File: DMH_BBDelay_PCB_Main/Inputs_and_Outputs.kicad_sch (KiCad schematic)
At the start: 13 parts, among them J10 TRS_Jack_6.35mm_Sw, J11 TRS_Jack_6.35mm_Sw, J12 TRS_Jack_6.35mm_Sw, J13 TRS_Jack_6.35mm_Sw, J14 TRS_Jack_6.35mm_Sw, J15 TRS_Jack_6.35mm_Sw, J16 TRS_Jack_6.35mm_Sw, J17 TRS_Jack_6.35mm_Sw, J18 TRS_Jack_6.35mm_Sw, J19 TRS_Jack_6.35mm_Sw, J20 TRS_Jack_6.35mm_Sw, J200 IDC_02x05, J21 TRS_Jack_6.35mm_Sw

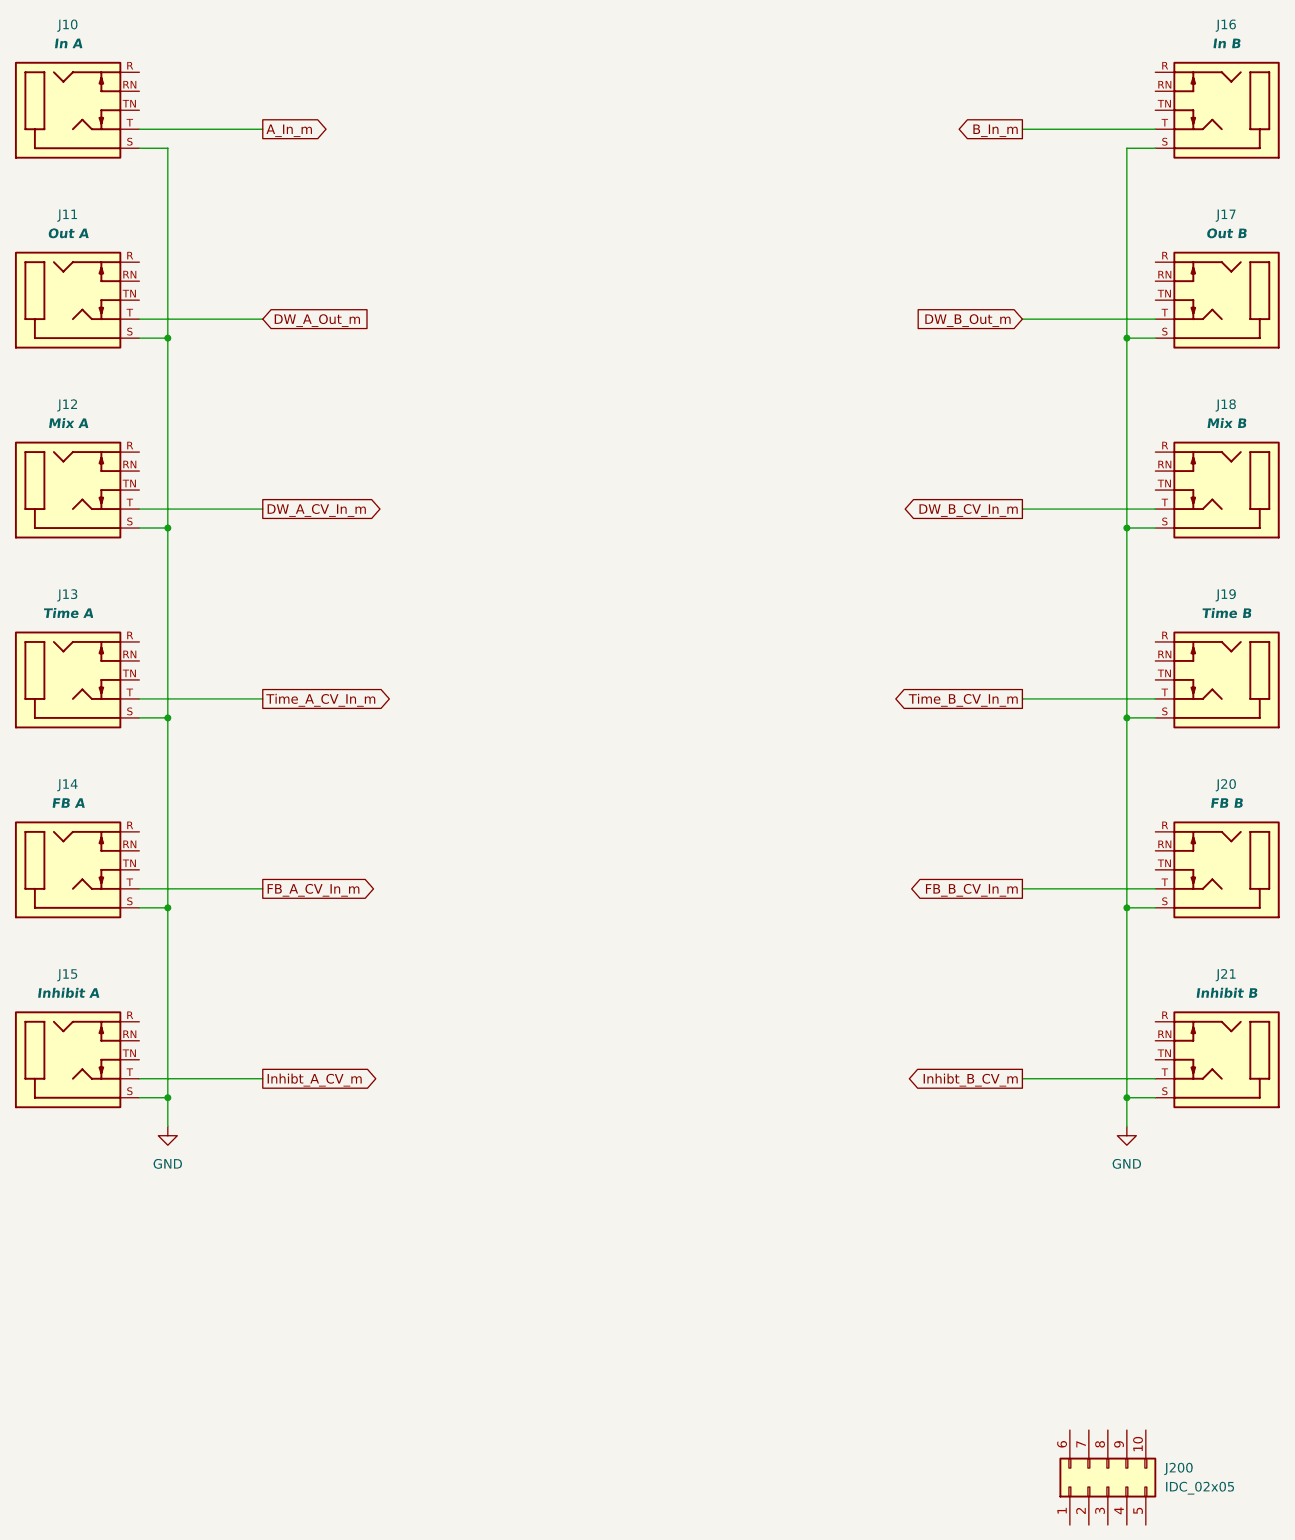
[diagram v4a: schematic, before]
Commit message: Added J200 connections in IO page
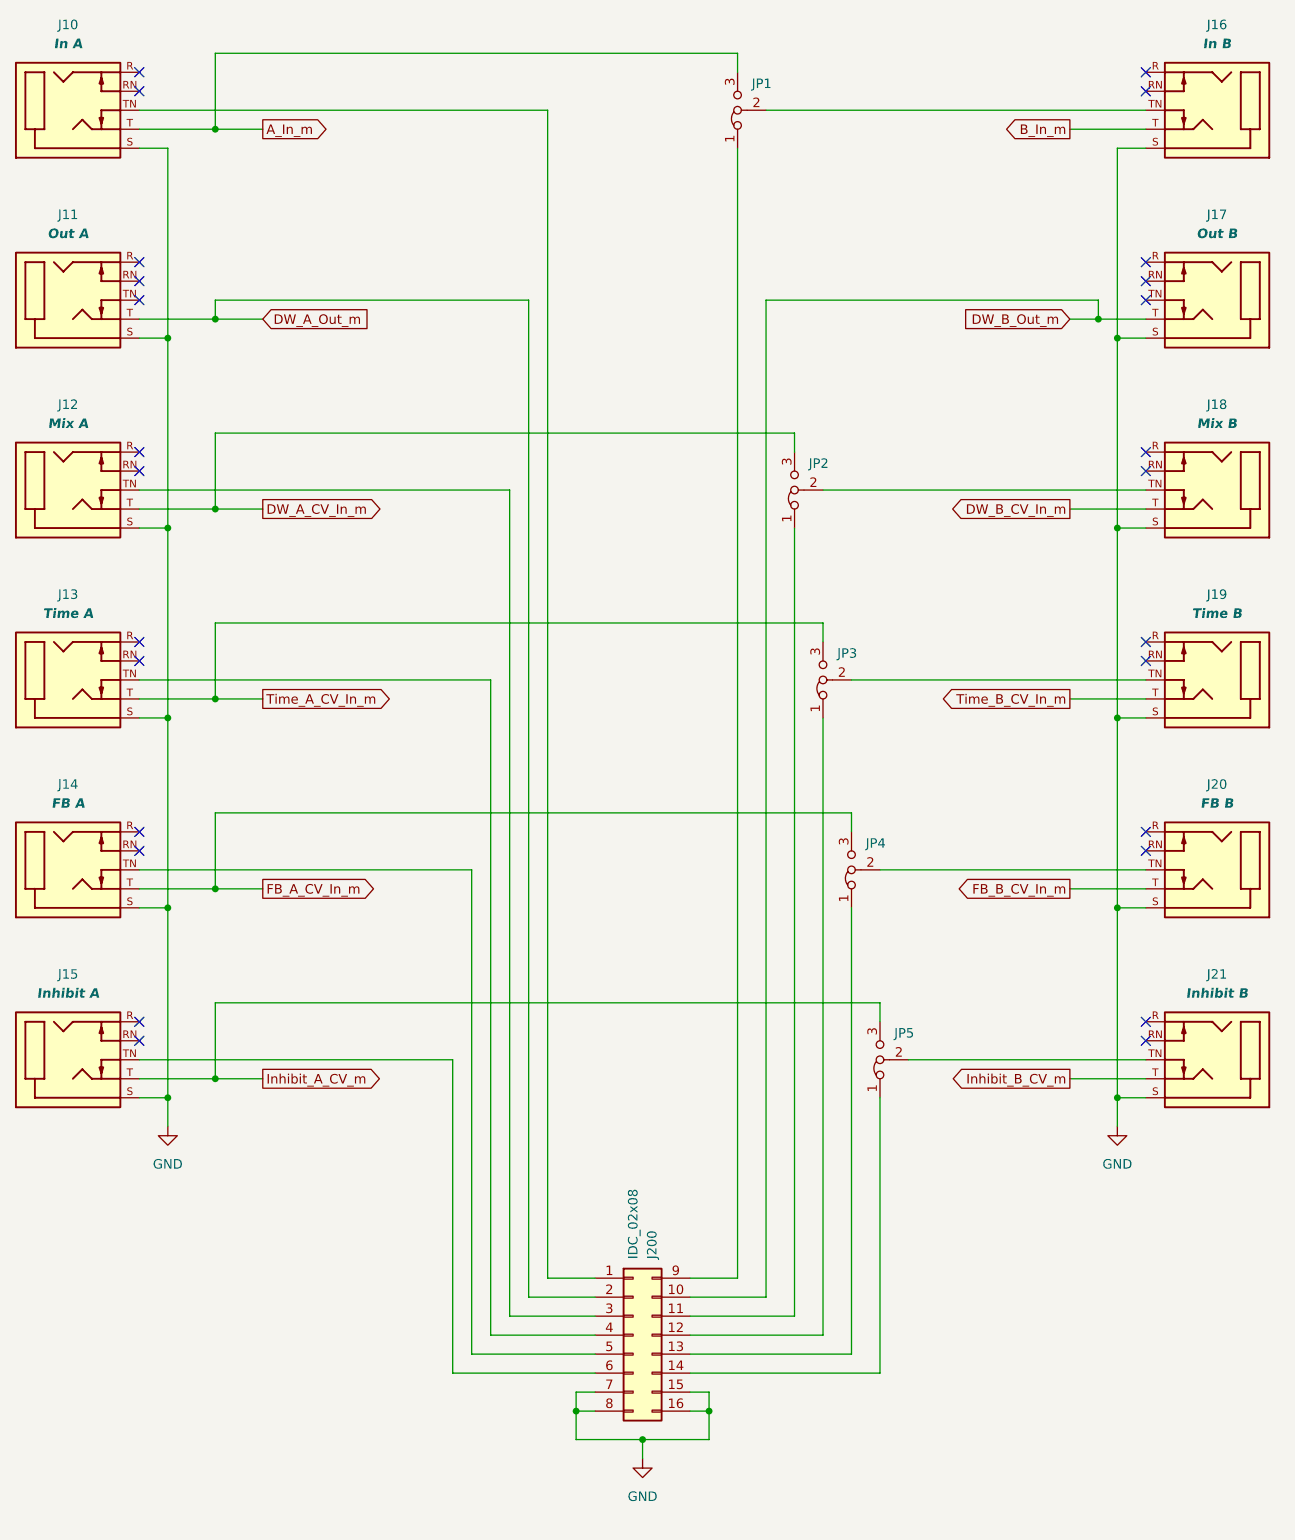
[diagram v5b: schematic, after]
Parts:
- removed J200: IDC_02x05, SynthStuff:IDC-Header_2x05_P2.54mm_Vertical_BackBone, symbol SynthStuff:BackBone_Connector_10Pin
- added J200: IDC_02x08, SynthStuff:IDC-Header_2x08_P2.54mm_Vertical_BackBone, symbol SynthStuff:BackBone_Connector_16Pin
- added JP1, JP2, JP3, JP4, JP5: Jumper_3_Bridged12, symbol Jumper:Jumper_3_Bridged12
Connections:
- net A_In_m: now also JP1.3 (B)
- net DW_A_CV_In_m: now also JP2.3 (B)
- net DW_A_Out_m: now also J200.2 (Pin_2)
- net DW_B_Out_m: now also J200.10 (Pin_10)
- net FB_A_CV_In_m: now also JP4.3 (B)
- net GND: now also J200.15 (Pin_15), J200.16 (Pin_16), J200.7 (Pin_7), J200.8 (Pin_8)
- net Time_A_CV_In_m: now also JP3.3 (B)
- net at J16.TN (2): now also JP1.2 (C)
- net at J14.TN (2): now also J200.5 (Pin_5)
- net at J19.TN (2): now also JP3.2 (C)
- net at J20.TN (2): now also JP4.2 (C)
- net at J21.TN (2): now also JP5.2 (C)
- net at J18.TN (2): now also JP2.2 (C)
- net at J13.TN (2): now also J200.4 (Pin_4)
- net at J10.TN (2): now also J200.1 (Pin_1)
- net at J12.TN (2): now also J200.3 (Pin_3)
- net at J15.TN (2): now also J200.6 (Pin_6)
- net Inhibt_A_CV_m renamed Inhibit_A_CV_m
- net Inhibit_A_CV_m: now also JP5.3 (B)
- net Inhibt_B_CV_m renamed Inhibit_B_CV_m
- new net: J200.14 (Pin_14), JP5.1 (A)
- new net: J200.12 (Pin_12), JP3.1 (A)
- new net: J200.11 (Pin_11), JP2.1 (A)
- new net: J200.13 (Pin_13), JP4.1 (A)
- new net: J200.9 (Pin_9), JP1.1 (A)
- no-connect marks 0 -> 26
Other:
- moved on the sheet: J16, J17, J18, J19, J20, J21

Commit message: Schematic ready for breadboarding
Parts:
- JP1, JP2, JP3, JP4, JP5: footprint (none) -> Connector_PinHeader_2.54mm:PinHeader_1x03_P2.54mm_Vertical
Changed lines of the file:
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@@
 			)
 		)
-		(property "Footprint" ""
+		(property "Footprint" "Connector_PinHeader_2.54mm:PinHeader_1x03_P2.54mm_Vertical"
 			(at 133.35 165.1 0)
 			(hide yes)
@@
 			)
 		)
-		(property "Footprint" ""
+		(property "Footprint" "Connector_PinHeader_2.54mm:PinHeader_1x03_P2.54mm_Vertical"
 			(at 125.73 114.3 0)
 			(hide yes)
@@
 			)
 		)
-		(property "Footprint" ""
+		(property "Footprint" "Connector_PinHeader_2.54mm:PinHeader_1x03_P2.54mm_Vertical"
 			(at 121.92 88.9 0)
 			(hide yes)
@@
 			)
 		)
-		(property "Footprint" ""
+		(property "Footprint" "Connector_PinHeader_2.54mm:PinHeader_1x03_P2.54mm_Vertical"
 			(at 114.3 38.1 0)
 			(hide yes)
@@
 			)
 		)
-		(property "Footprint" ""
+		(property "Footprint" "Connector_PinHeader_2.54mm:PinHeader_1x03_P2.54mm_Vertical"
 			(at 129.54 139.7 0)
 			(hide yes)

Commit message: Synced channel A and B schematics
... and applied several minor improvements and optimizations.
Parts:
- JP1, JP2, JP3, JP4, JP5: now in the parts list
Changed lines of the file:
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@@
 		(body_style 1)
 		(exclude_from_sim no)
-		(in_bom no)
+		(in_bom yes)
 		(on_board yes)
 		(in_pos_files yes)
@@
 		(body_style 1)
 		(exclude_from_sim no)
-		(in_bom no)
+		(in_bom yes)
 		(on_board yes)
 		(in_pos_files yes)
@@
 		(body_style 1)
 		(exclude_from_sim no)
-		(in_bom no)
+		(in_bom yes)
 		(on_board yes)
 		(in_pos_files yes)
@@
 		(body_style 1)
 		(exclude_from_sim no)
-		(in_bom no)
+		(in_bom yes)
 		(on_board yes)
 		(in_pos_files yes)
@@
 		(body_style 1)
 		(exclude_from_sim no)
-		(in_bom no)
-		(on_board yes)
-		(in_pos_files yes)
+		(in_bom yes)
+		(on_board yes)
+		(in_pos_files yes)
